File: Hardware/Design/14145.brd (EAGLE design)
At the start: 60.3 x 53.3 mm, 103 parts, among them J1 B, J2 RJ45J, J3 PBC10SAAN, J4 RJ45J, J5 PBC10SAAN, J6 PBC10SAAN, J7 PBC08SAAN, J8 PPPC032LFBN, Q1 DMB, Q2 K38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

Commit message: Hardware: ^4 review
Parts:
- removed C13: 0.1uF, C-C:C0603(1608)
- removed D1: SQ4, D-SBR:SMA
- removed R19: 200k, R-C:C0805(2012)
- removed R20: 10k, R-C:C0805(2012)
- added TP13, TP14, TP8: TPPAD1-08, J-TP:P1-08
- moved R11 10.2 mm to (14.0, 4.70), turned to 180 degrees
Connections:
- removed net VIN: D1.K, J7.1, R19.1, U5.1, U5.3
- removed net VIN_ADC7: C13.1, R19.2, R20.1, U7.22
- new net N$1: TP8.TP, U7.12
- net +5V: now also U5.1, U5.3; no longer D1.A, R11.1
- net 0V: no longer C13.2, R20.2
- net DTR_RXD: now also TP14.TP; no longer U7.12
- net DTR_TXD: now also TP13.TP
- net IOREF: now also R11.1
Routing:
- net VIN: track 50.3 -> 0.00 mm, vias 1 -> 0
- net VIN_ADC7: track 35.4 -> 0.00 mm, vias 2 -> 0
- net +5V: track 71.7 -> 83.8 mm, vias 5 -> 8
- net N$1: track 0.00 -> 10.3 mm, vias 0 -> 1
- net MOSI: track 47.8 -> 52.9 mm
- net DTR_RXD: track 90.6 -> 85.8 mm, vias 5 -> 4
- net FTDI_TX: track 60.3 -> 57.3 mm
- net TX: track 112.8 -> 115.2 mm, vias 4 -> 5
- net IOREF: track 98.9 -> 101.2 mm
- net DTR_TXD: track 39.9 -> 38.3 mm
- net !SS!: track 30.2 -> 31.4 mm
- net USB5V_ADC6: track 39.0 -> 38.1 mm
- net MISO: track 41.6 -> 42.4 mm
- net SCK: track 68.8 -> 69.4 mm
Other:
- board text added: "14145^4"
- board text added: "DTR RXD"
- board text added: "DTR TXD"
- board text added: "ICP1"
- board text added: "RPUBUS.ORG"
- board text removed: "14145^3"
- board text removed: "EPCCS.ORG"

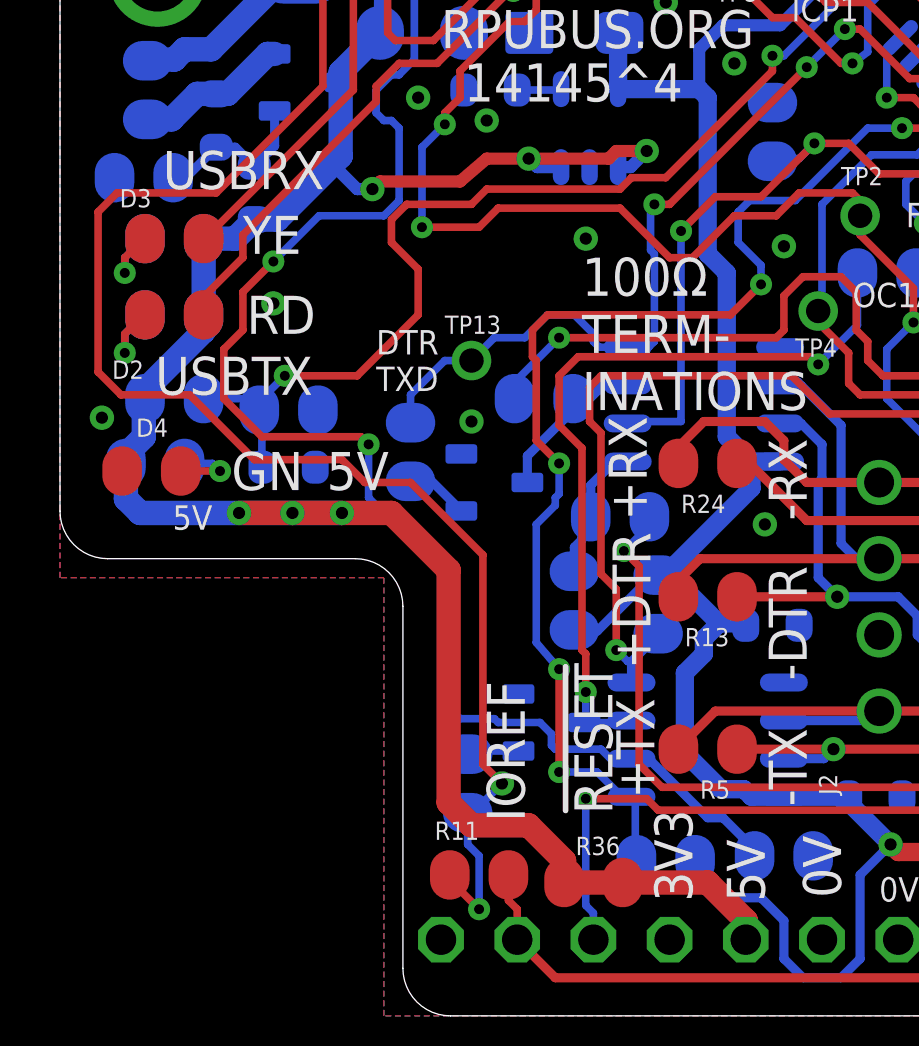
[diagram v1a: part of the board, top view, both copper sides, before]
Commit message: Hardware: arrange parts and their references
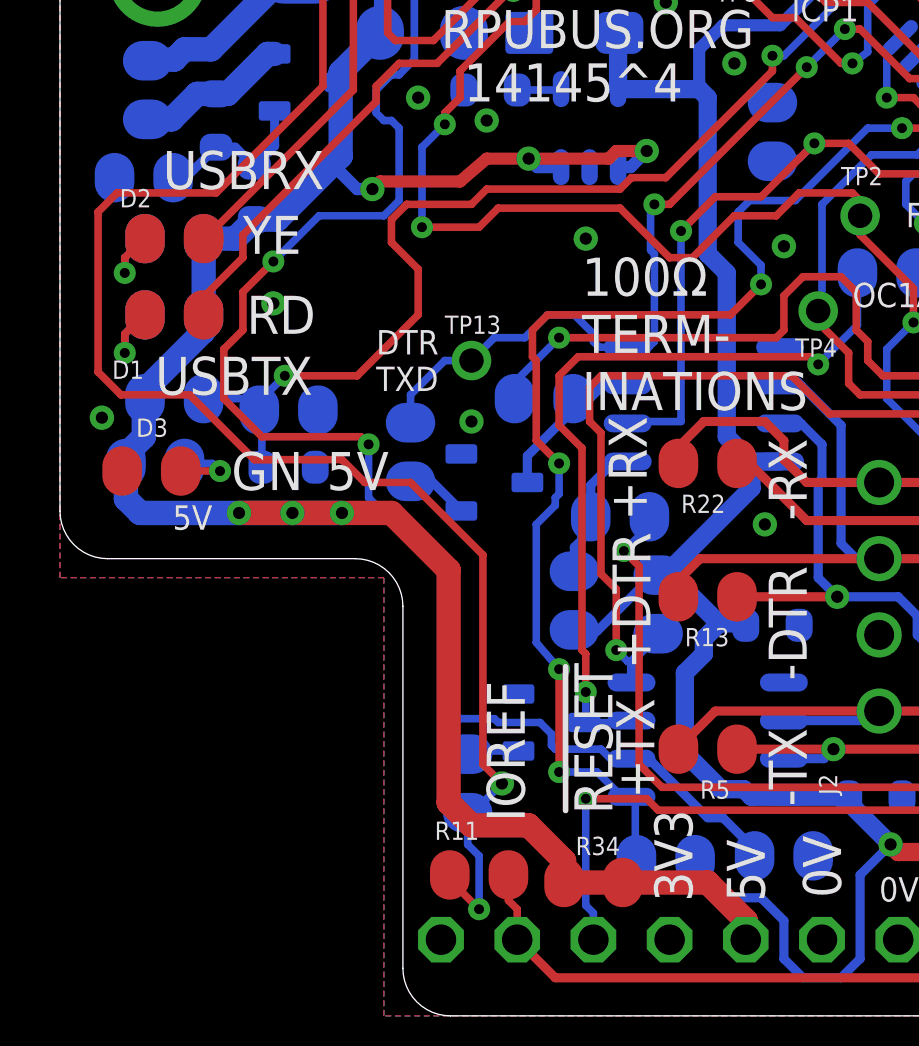
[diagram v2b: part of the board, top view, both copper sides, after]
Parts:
- removed C19: .1uF, C-C:C0603(1608)
- removed D5: T4, D-GP:SOD123
- removed R36: JMP, R-C:C0805(2012)
- removed R37: 1.5k, R-C:C0805(2012)
- added C13: 470pF, C-C:C0603(1608)
- added D1: 0805RD, D-LED:C0805(2012)
- added R19, R20: 1.5k, R-C:C0805(2012)
- C14: value 470pF -> 10uF; device C-C:C0603(1608) -> C-T:3216
- C15: value 10uF -> .1uF; device C-T:3216 -> C-C:C0603(1608)
- D2: value 0805RD -> 0805YE
- D3: value 0805YE -> 0805GN
- D4: value 0805GN -> T4; device D-LED:C0805(2012) -> D-GP:SOD123
- R22: value 1.5k -> 100
- R23: value 1.5k -> 10k
- R24: value 100 -> 3.01k
- R25: value 10k -> 100
- R26: value 3.01k -> 10K
- R27: value 100 -> 182
- R28, R31: value 10K -> 3.01k
- R29: value 182 -> 10K
- R32, R33: value 3.01k -> 182
- R34: value 182 -> JMP
- R35: value 182 -> 1.5k
- Y1: value 14.7456MHz -> 12MHz
- moved D4 56.5 mm to (55.6, 38.7), flipped to the bottom, turned to 180 degrees
- moved R35 49.9 mm to (56.5, 33.0), turned to 180 degrees
- moved R34 45.1 mm to (17.8, 4.45), flipped to the top, turned to 180 degrees
- moved R28 42.5 mm to (32.6, 8.38), turned to 90 degrees
- moved R30 40.1 mm to (42.0, 47.4), turned to 270 degrees
- moved R23 39.2 mm to (40.6, 6.99), turned to 180 degrees
- moved R27 36.7 mm to (50.5, 47.9)
- moved R33 33.7 mm to (8.51, 46.6), turned to 0 degrees
- moved R32 33.4 mm to (8.64, 48.6), turned to 0 degrees
- moved R26 28.3 mm to (47.8, 48.1), turned to 180 degrees
- moved C15 25.1 mm to (42.2, 35.1), turned to 90 degrees
- moved R22 19.3 mm to (21.6, 18.4), flipped to the top, turned to 0 degrees
- moved R24 18.7 mm to (40.1, 20.8), flipped to the bottom
- moved C16 16.3 mm to (25.9, 36.2), turned to 0 degrees
- moved R31 16.2 mm to (42.0, 43.4), turned to 270 degrees
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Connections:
- net +3V3: now also C14.+, C15.1, D4.C, R23.2, R29.2, R30.1, R31.1, R35.1; no longer C15.+, C18.1, D5.C, R25.2, R31.2, R32.1, R33.1, R37.1
- net +5V: now also R19.2, R20.2, R34.1, R34.2; no longer R22.2, R23.2, R36.1, R36.2
- net +RX: now also R22.1; no longer R24.1
- net -RX: now also R22.2; no longer R24.2
- net 0V: now also C13.2, C14.-, C15.2, D3.K, R24.2; no longer C14.2, C15.-, C19.2, D4.K, R26.2
- net FTDI_TX: now also R25.1; no longer R27.1
- net IOREF: now also R26.1; no longer R28.1
- net MGR_!RESET: now also D4.A, R29.1; no longer D5.A, R31.1
- net N$10: now also R26.2, R27.2; no longer R28.2, R29.2
- net N$11: now also R28.2; no longer R30.2
- net N$14: now also D3.A, R21.1; no longer D4.A, R23.1
- net N$16: now also D1.A, R19.1; no longer D2.A, R21.1
- net N$24: now also C13.1; no longer C14.1
- net N$25: now also R25.2; no longer R27.2
- net N$29: now also R35.2; no longer R37.2
- net N$6: now also D2.A, R20.1; no longer D3.A, R22.1
- net N$7: now also D1.K; no longer D2.K
- net N$8: now also D2.K; no longer D3.K
- net RPU_AREF: now also C18.1; no longer C19.1
- net RX: now also R27.1; no longer R29.1
- net RX_!RE: now also R24.1; no longer R26.1
- net RX_DE: now also R28.1; no longer R30.1
- net RX_RPU: now also R23.1; no longer R25.1
- net SCL: now also R33.2; no longer R35.2
- net SCL0: now also R31.2, R33.1; no longer R33.2, R35.1
- net SDA: now also R32.2; no longer R34.2
- net SDA0: now also R30.2, R32.1; no longer R32.2, R34.1
